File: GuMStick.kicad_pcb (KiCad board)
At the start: 2 copper layers, 20 x 66.2 mm, 35 parts, among them Q1 SI2302, SW1 K3-1235S, SW2 K3-1235S, U1 XIAO-nRF52840-SMD, U2 Wio-SX1262, U3 M20-7910442R, U5 BQ25606RGER

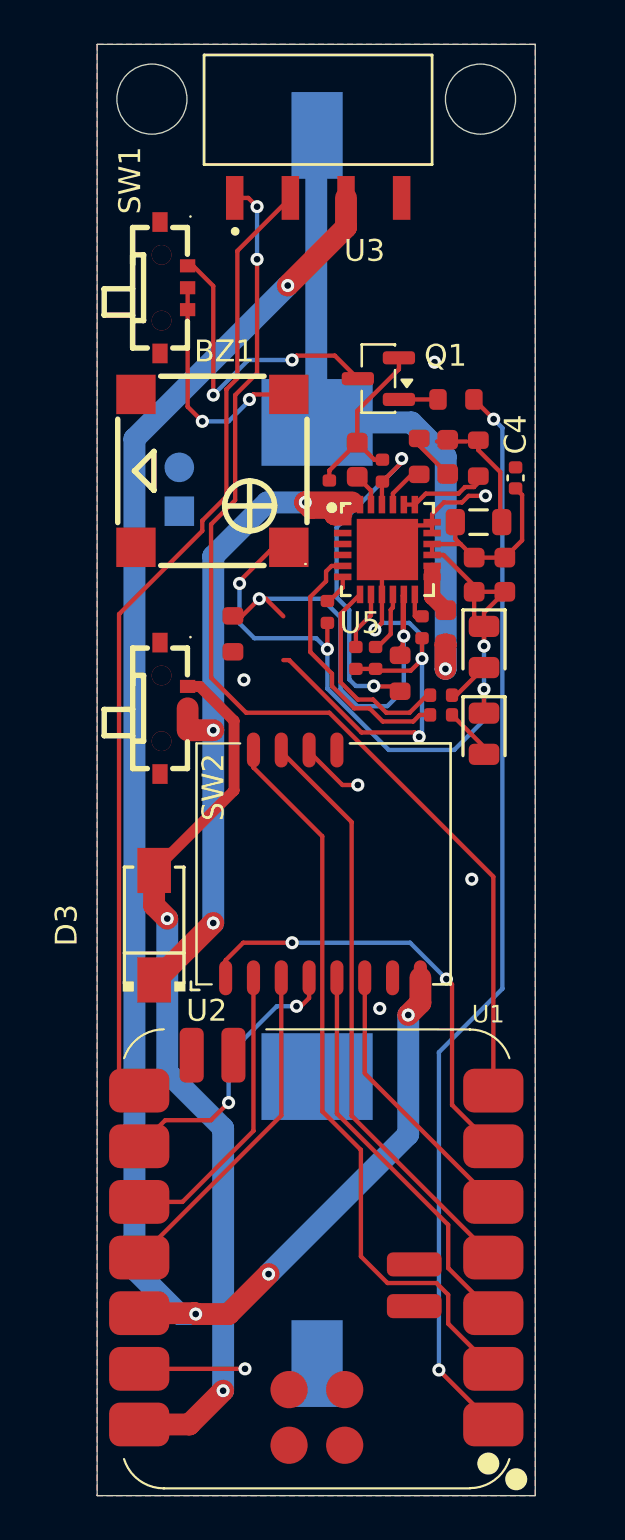
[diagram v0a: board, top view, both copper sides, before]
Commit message: PCB updated to include reverse polarity protection via MOSFET, added diode to battery pin on XIAO to allow battery voltage detection without allowing charging.
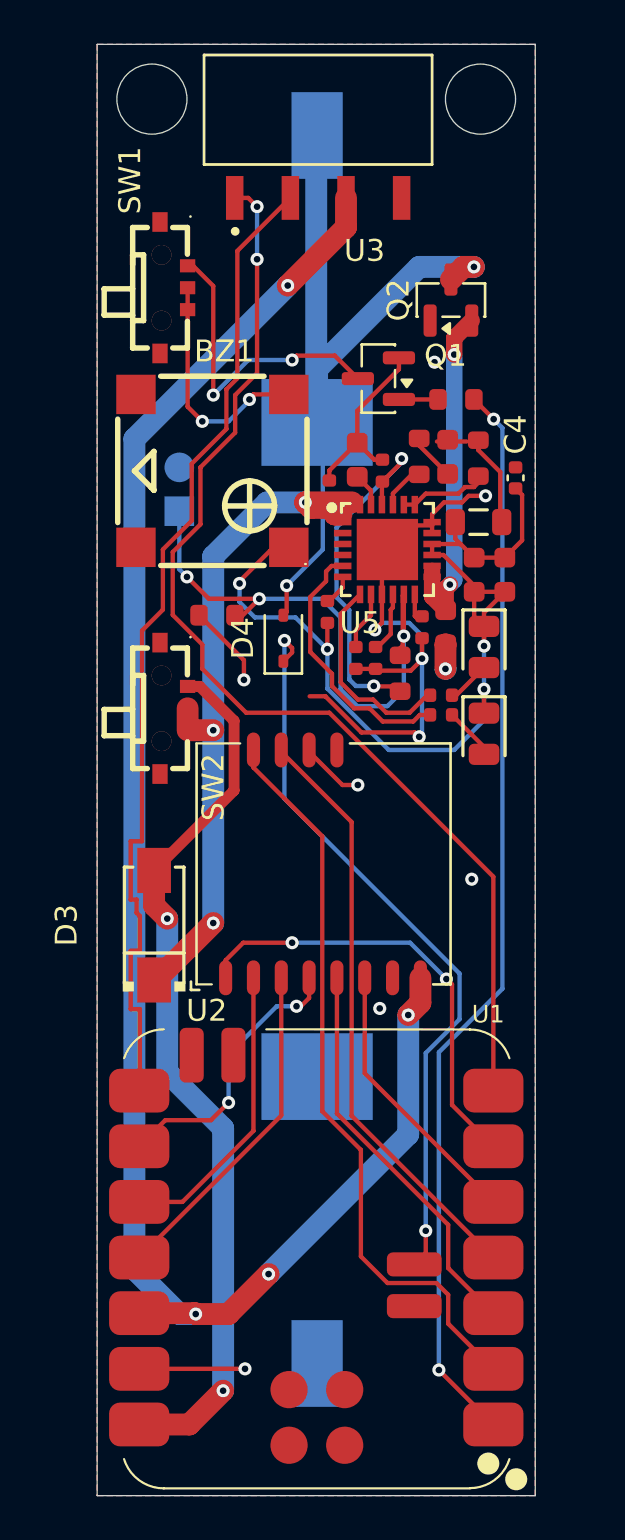
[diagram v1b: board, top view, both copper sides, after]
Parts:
- added D4: 1N5819WS, Diode_SMD:D_SOD-323, F.Cu at (148.5, 106.4)
- added Q2: SI2302, Package_TO_SOT_SMD:SOT-23, F.Cu at (156.2, 91.0)
- R22: value 330Ω -> 680Ω
- moved R18 1.12 mm to (145.5, 105.3), turned to 180 degrees
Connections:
- net Net-(C7-Pad1) renamed RPP S
- C7 pad 2: BAT+ -> GND
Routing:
- net Net-(D4-K): track 0.00 -> 33.9 mm, vias 0 -> 2
- net RPP S: track 2.05 -> 15.8 mm, vias 0 -> 2
- net Net-(U5-TS): track 21.3 -> 26.7 mm, vias 2 -> 3
- net BAT+: track 30.5 -> 35.6 mm, vias 1 -> 2
- net GND: track 45.3 -> 48.3 mm, vias 10 -> 11
- net SDA: track 50.0 -> 51.4 mm
- net SCL: track 44.4 -> 45.3 mm
- net SYS: track 44.6 -> 44.0 mm

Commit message: Removed 180R on buzzer
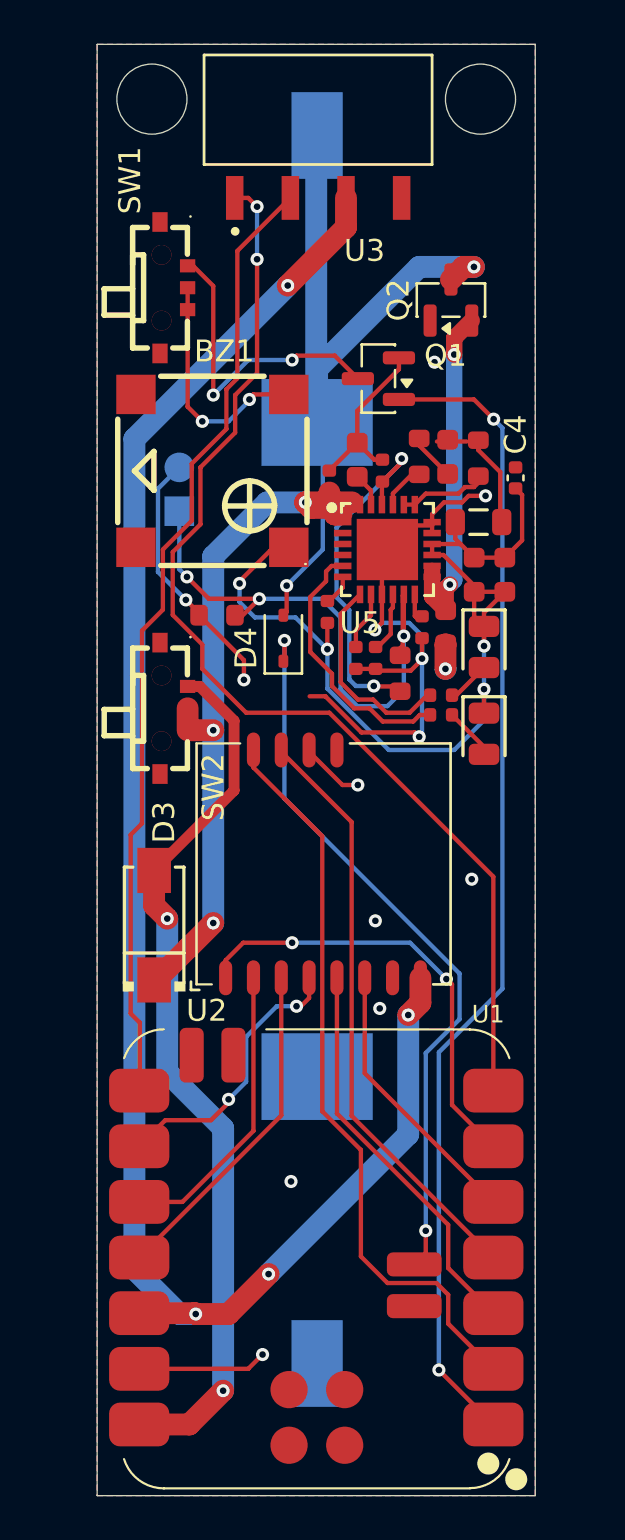
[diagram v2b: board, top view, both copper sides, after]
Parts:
- removed R1: 180Ω, PCM_JLCPCB:R_0603
- C2: value 1uF 0402 -> 1uF
- C4: value Unpopulated -> C4 DNP
- TH1: value Thermistor_NTC 103AT -> DNP NTC 103AT
- moved C2 0.45 mm to (150.6, 99.2)
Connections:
- Q1 pad 1: Net-(Q1-G) -> BUZ_PWM
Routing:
- net GND: track 48.3 -> 56.9 mm, vias 11 -> 14
- net BUZ_PWM: track 49.6 -> 53.0 mm
- net Net-(Q1-G): track 1.78 -> 0.00 mm
- net SCL: track 45.3 -> 44.0 mm
- net VBUS: track 32.0 -> 32.8 mm

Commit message: Fixes to part numbers and details
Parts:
- D4: footprint Diode_SMD:D_SOD-323 -> easyeda2kicad:SOD-323_L1.8-W1.3-LS2.5-RD
- L1: value 1uH,50mA -> 1uH,1A
- Q1, Q2: footprint Package_TO_SOT_SMD:SOT-23 -> easyeda2kicad:SOT-23_L2.9-W1.3-P1.90-LS2.4-BR
- TH1: value DNP NTC 103AT -> Thermistor_NTC 103AT
- moved Q1 0.21 mm to (153.1, 94.5), turned to 0 degrees
- moved D4 0.07 mm to (148.6, 106.3)
- moved Q2 0.06 mm to (156.1, 91.0), turned to -90 degrees
- moved R22 0.06 mm to (152.7, 107.3)

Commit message: Updating to current builds. Firmware has base messaging functionality. Buzzer still presents issues, possibly due to the capacitor/inductor setup on SYS as the D0 pin should turn on the mosfet to put the buzzer in circuit with SYS voltage and ground.
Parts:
- U3: value M20-7910442R -> MF254RS-11-04-0743
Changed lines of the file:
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@@
 				(font
 					(size 1.27 1.27)
+					(thickness 0.15)
 				)
 			)
@@
 				(font
 					(size 1.27 1.27)
+					(thickness 0.15)
 				)
 			)
@@
 				(font
 					(size 1.27 1.27)
+					(thickness 0.15)
 				)
 			)
@@
 			)
 		)
-		(property "Value" "M20-7910442R"
+		(property "Value" "MF254RS-11-04-0743"
 			(at 0.06 2.775 180)
 			(layer "F.Fab")
@@
 	)
 	(segment
-		(start 156.725 89.45)
-		(end 156.15 90.025)
-		(width 1)
-		(layer "F.Cu")
-		(net "BAT+")
-	)
-	(segment
-		(start 148.65 104)
-		(end 148.65 105.2)
-		(width 0.2)
-		(layer "F.Cu")
-		(net "BAT+")
-	)
-	(segment
-		(start 148.65 105.2)
-		(end 148.5 105.35)
-		(width 0.2)
-		(layer "F.Cu")
-		(net "BAT+")
-	)
-	(segment
-		(start 157.2 89.45)
-		(end 156.725 89.45)
-		(width 1)
-		(layer "F.Cu")
-		(net "BAT+")
-	)
-	(via
-		(at 148.65 104)
-		(size 0.6)
-		(drill 0.3)
-		(layers "F.Cu" "B.Cu")
-		(net "BAT+")
-	)
-	(via
-		(at 157.2 89.45)
-		(size 0.6)
-		(drill 0.3)
-		(layers "F.Cu" "B.Cu")
-		(net "BAT+")
-	)
-	(segment
-		(start 154.7 89.45)
-		(end 157.2 89.45)
-		(width 1)
-		(layer "B.Cu")
-		(net "BAT+")
-	)
-	(segment
-		(start 150.04 96.55)
-		(end 150.3 96.81)
-		(width 0.2)
-		(layer "B.Cu")
-		(net "BAT+")
-	)
-	(segment
-		(start 150.04 94.11)
-		(end 154.7 89.45)
-		(width 1)
-		(layer "B.Cu")
-		(net "BAT+")
-	)
-	(segment
-		(start 150.3 96.81)
-		(end 150.3 102.35)
-		(width 0.2)
-		(layer "B.Cu")
-		(net "BAT+")
-	)
-	(segment
-		(start 150 83.49)
-		(end 150.04 83.45)
-		(width 1)
-		(layer "B.Cu")
-		(net "BAT+")
-	)
-	(segment
-		(start 150.04 96.55)
-		(end 150.04 94.11)
-		(width 1)
-		(layer "B.Cu")
-		(net "BAT+")
-	)
-	(segment
-		(start 150.04 96.55)
-		(end 150 96.51)
-		(width 1)
-		(layer "B.Cu")
-		(net "BAT+")
-	)
-	(segment
-		(start 150.3 102.35)
-		(end 148.65 104)
-		(width 0.2)
-		(layer "B.Cu")
-		(net "BAT+")
-	)
-	(segment
-		(start 150 96.51)
-		(end 150 83.49)
-		(width 1)
-		(layer "B.Cu")
-		(net "BAT+")
-	)
-	(segment
 		(start 156.4 109)
 		(end 157.66 107.74)
@@
 	)
 	(segment
+		(start 153.4 106.21)
+		(end 153.4 105.1)
+		(width 0.2)
+		(layer "F.Cu")
+		(net "Net-(U5-ICHG)")
+	)
+	(segment
+		(start 152.71 106.9)
+		(end 153.4 106.21)
+		(width 0.2)
+		(layer "F.Cu")
+		(net "Net-(U5-ICHG)")
+	)
+	(segment
+		(start 153.5 105)
+		(end 153.5 104.4)
+		(width 0.2)
+		(layer "F.Cu")
+		(net "Net-(U5-ICHG)")
+	)
+	(segment
+		(start 153.4 105.1)
+		(end 153.5 105)
+		(width 0.2)
+		(layer "F.Cu")
+		(net "Net-(U5-ICHG)")
+	)
+	(segment
 		(start 150.85 93.5)
 		(end 149.1 93.5)
@@
 	)
 	(segment
-		(start 153.4 106.21)
-		(end 153.4 105.1)
-		(width 0.2)
-		(layer "F.Cu")
-		(net "Net-(U5-ICHG)")
-	)
-	(segment
-		(start 152.71 106.9)
-		(end 153.4 106.21)
-		(width 0.2)
-		(layer "F.Cu")
-		(net "Net-(U5-ICHG)")
-	)
-	(segment
-		(start 153.5 105)
-		(end 153.5 104.4)
-		(width 0.2)
-		(layer "F.Cu")
-		(net "Net-(U5-ICHG)")
-	)
-	(segment
-		(start 153.4 105.1)
-		(end 153.5 105)
-		(width 0.2)
-		(layer "F.Cu")
-		(net "Net-(U5-ICHG)")
-	)
-	(segment
 		(start 144.13 95.83)
 		(end 144.13 91.4)
@@
 		(net "Net-(C6-Pad2)")
 	)
+	(segment
+		(start 156.725 89.45)
+		(end 156.15 90.025)
+		(width 1)
+		(layer "F.Cu")
+		(net "BAT+")
+	)
+	(segment
+		(start 148.65 104)
+		(end 148.65 105.2)
+		(width 0.2)
+		(layer "F.Cu")
+		(net "BAT+")
+	)
+	(segment
+		(start 148.65 105.2)
+		(end 148.5 105.35)
+		(width 0.2)
+		(layer "F.Cu")
+		(net "BAT+")
+	)
+	(segment
+		(start 157.2 89.45)
+		(end 156.725 89.45)
+		(width 1)
+		(layer "F.Cu")
+		(net "BAT+")
+	)
+	(via
+		(at 148.65 104)
+		(size 0.6)
+		(drill 0.3)
+		(layers "F.Cu" "B.Cu")
+		(net "BAT+")
+	)
+	(via
+		(at 157.2 89.45)
+		(size 0.6)
+		(drill 0.3)
+		(layers "F.Cu" "B.Cu")
+		(net "BAT+")
+	)
+	(segment
+		(start 154.7 89.45)
+		(end 157.2 89.45)
+		(width 1)
+		(layer "B.Cu")
+		(net "BAT+")
+	)
+	(segment
+		(start 150.04 96.55)
+		(end 150.3 96.81)
+		(width 0.2)
+		(layer "B.Cu")
+		(net "BAT+")
+	)
+	(segment
+		(start 150.04 94.11)
+		(end 154.7 89.45)
+		(width 1)
+		(layer "B.Cu")
+		(net "BAT+")
+	)
+	(segment
+		(start 150.3 96.81)
+		(end 150.3 102.35)
+		(width 0.2)
+		(layer "B.Cu")
+		(net "BAT+")
+	)
+	(segment
+		(start 150 83.49)
+		(end 150.04 83.45)
+		(width 1)
+		(layer "B.Cu")
+		(net "BAT+")
+	)
+	(segment
+		(start 150.04 96.55)
+		(end 150.04 94.11)
+		(width 1)
+		(layer "B.Cu")
+		(net "BAT+")
+	)
+	(segment
+		(start 150.04 96.55)
+		(end 150 96.51)
+		(width 1)
+		(layer "B.Cu")
+		(net "BAT+")
+	)
+	(segment
+		(start 150.3 102.35)
+		(end 148.65 104)
+		(width 0.2)
+		(layer "B.Cu")
+		(net "BAT+")
+	)
+	(segment
+		(start 150 96.51)
+		(end 150 83.49)
+		(width 1)
+		(layer "B.Cu")
+		(net "BAT+")
+	)
 	(zone
